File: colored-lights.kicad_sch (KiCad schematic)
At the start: 8 parts, among them Q1 FQP30N06L-ND, Q2 FQP30N06L-ND, Q3 FQP30N06L-ND, Q4 FQP30N06L-ND

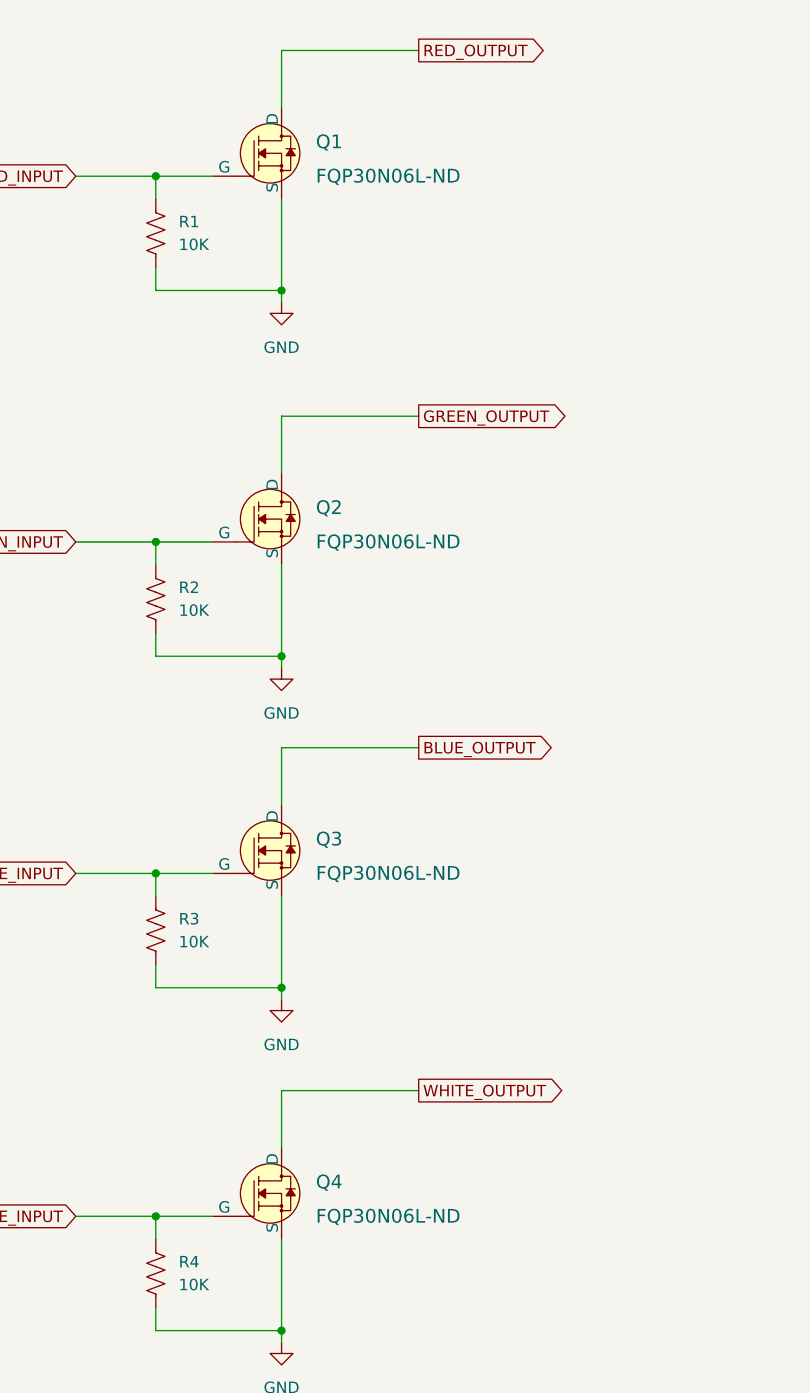
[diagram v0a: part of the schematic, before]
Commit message: changed to SO-8 MOSFETs
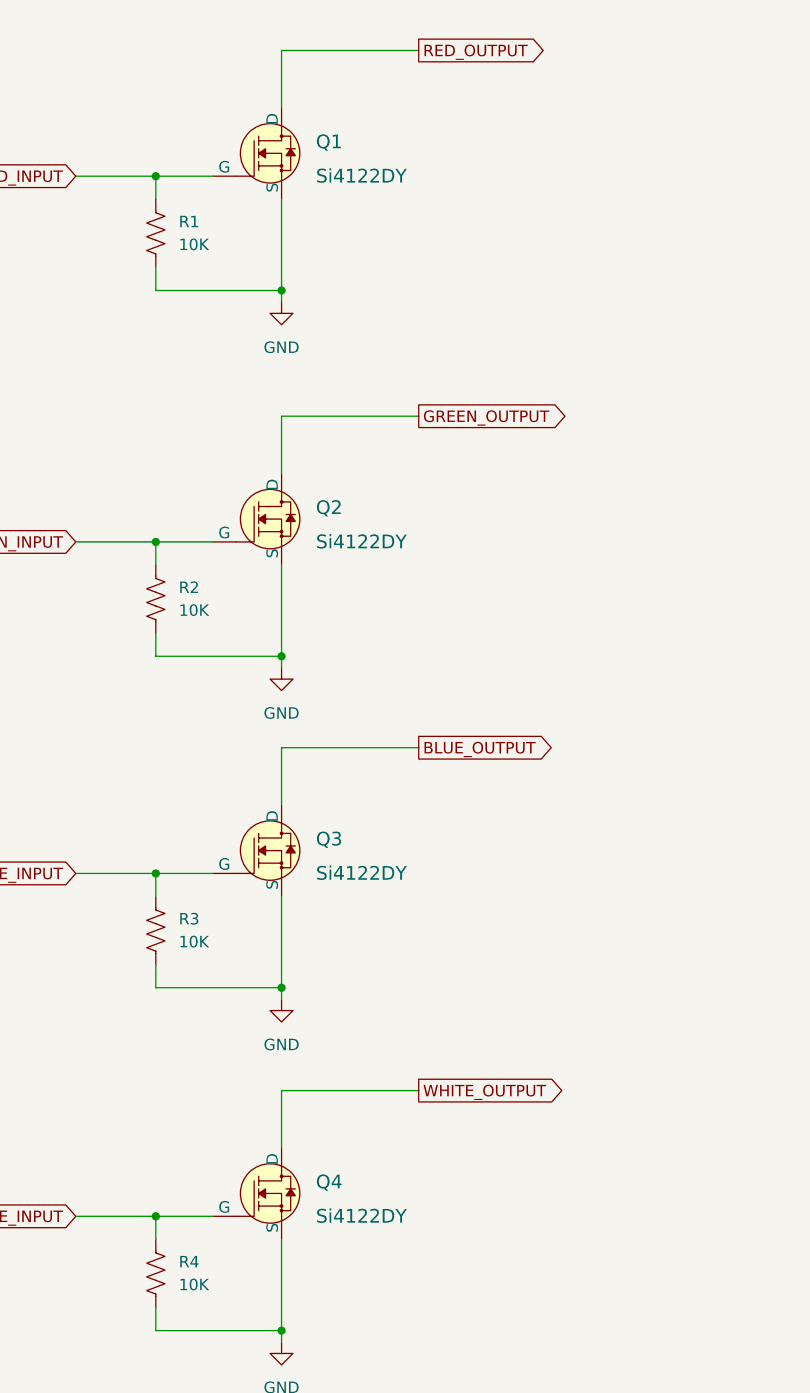
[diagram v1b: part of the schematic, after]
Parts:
- Q1, Q2, Q3, Q4: value FQP30N06L-ND -> Si4122DY; footprint Package_TO_SOT_THT:TO-220-3_Vertical -> Library:SOIC-8_3.9x4.9mm_P1.27mm transistor
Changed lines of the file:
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@@
       (effects (font (size 1.524 1.524)) (justify left))
     )
-    (property "Value" "FQP30N06L-ND" (id 1) (at 88.9 115.57 0)
-      (effects (font (size 1.524 1.524)) (justify left))
-    )
-    (property "Footprint" "Package_TO_SOT_THT:TO-220-3_Vertical" (id 2) (at 90.805 105.2576 0)
+    (property "Value" "Si4122DY" (id 1) (at 88.9 115.57 0)
+      (effects (font (size 1.524 1.524)) (justify left))
+    )
+    (property "Footprint" "Library:SOIC-8_3.9x4.9mm_P1.27mm transistor" (id 2) (at 90.805 105.2576 0)
       (effects (font (size 1.524 1.524)) (justify left) hide)
     )
@@
       (effects (font (size 1.524 1.524)) (justify left))
     )
-    (property "Value" "FQP30N06L-ND" (id 1) (at 88.9 153.67 0)
-      (effects (font (size 1.524 1.524)) (justify left))
-    )
-    (property "Footprint" "Package_TO_SOT_THT:TO-220-3_Vertical" (id 2) (at 90.805 143.3576 0)
+    (property "Value" "Si4122DY" (id 1) (at 88.9 153.67 0)
+      (effects (font (size 1.524 1.524)) (justify left))
+    )
+    (property "Footprint" "Library:SOIC-8_3.9x4.9mm_P1.27mm transistor" (id 2) (at 90.805 143.3576 0)
       (effects (font (size 1.524 1.524)) (justify left) hide)
     )
@@
       (effects (font (size 1.524 1.524)) (justify left))
     )
-    (property "Value" "FQP30N06L-ND" (id 1) (at 88.9 78.74 0)
-      (effects (font (size 1.524 1.524)) (justify left))
-    )
-    (property "Footprint" "Package_TO_SOT_THT:TO-220-3_Vertical" (id 2) (at 90.805 68.4276 0)
+    (property "Value" "Si4122DY" (id 1) (at 88.9 78.74 0)
+      (effects (font (size 1.524 1.524)) (justify left))
+    )
+    (property "Footprint" "Library:SOIC-8_3.9x4.9mm_P1.27mm transistor" (id 2) (at 90.805 68.4276 0)
       (effects (font (size 1.524 1.524)) (justify left) hide)
     )
@@
       (effects (font (size 1.524 1.524)) (justify left))
     )
-    (property "Value" "FQP30N06L-ND" (id 1) (at 88.9 38.1 0)
-      (effects (font (size 1.524 1.524)) (justify left))
-    )
-    (property "Footprint" "Package_TO_SOT_THT:TO-220-3_Vertical" (id 2) (at 90.805 27.7876 0)
+    (property "Value" "Si4122DY" (id 1) (at 88.9 38.1 0)
+      (effects (font (size 1.524 1.524)) (justify left))
+    )
+    (property "Footprint" "Library:SOIC-8_3.9x4.9mm_P1.27mm transistor" (id 2) (at 90.805 27.7876 0)
       (effects (font (size 1.524 1.524)) (justify left) hide)
     )
@@
     )
     (path "/c5f897e2-09cf-4f35-a17a-84049b90b7bb"
-      (reference "Q1") (unit 1) (value "FQP30N06L-ND") (footprint "Package_TO_SOT_THT:TO-220-3_Vertical")
+      (reference "Q1") (unit 1) (value "Si4122DY") (footprint "Library:SOIC-8_3.9x4.9mm_P1.27mm transistor")
     )
     (path "/338da271-ee00-4323-a936-104caac63c0e"
-      (reference "Q2") (unit 1) (value "FQP30N06L-ND") (footprint "Package_TO_SOT_THT:TO-220-3_Vertical")
+      (reference "Q2") (unit 1) (value "Si4122DY") (footprint "Library:SOIC-8_3.9x4.9mm_P1.27mm transistor")
     )
     (path "/21abaf01-59ce-489b-ba58-2406d95a0e9b"
-      (reference "Q3") (unit 1) (value "FQP30N06L-ND") (footprint "Package_TO_SOT_THT:TO-220-3_Vertical")
+      (reference "Q3") (unit 1) (value "Si4122DY") (footprint "Library:SOIC-8_3.9x4.9mm_P1.27mm transistor")
     )
     (path "/2d96a81f-c9dd-46c0-a0c5-537d6fda6c5c"
-      (reference "Q4") (unit 1) (value "FQP30N06L-ND") (footprint "Package_TO_SOT_THT:TO-220-3_Vertical")
+      (reference "Q4") (unit 1) (value "Si4122DY") (footprint "Library:SOIC-8_3.9x4.9mm_P1.27mm transistor")
     )
     (path "/44d7adbf-1ae3-4a83-84eb-040e4c81422a"
